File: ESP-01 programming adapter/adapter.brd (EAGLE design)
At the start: 27 x 27.3 mm, 7 parts

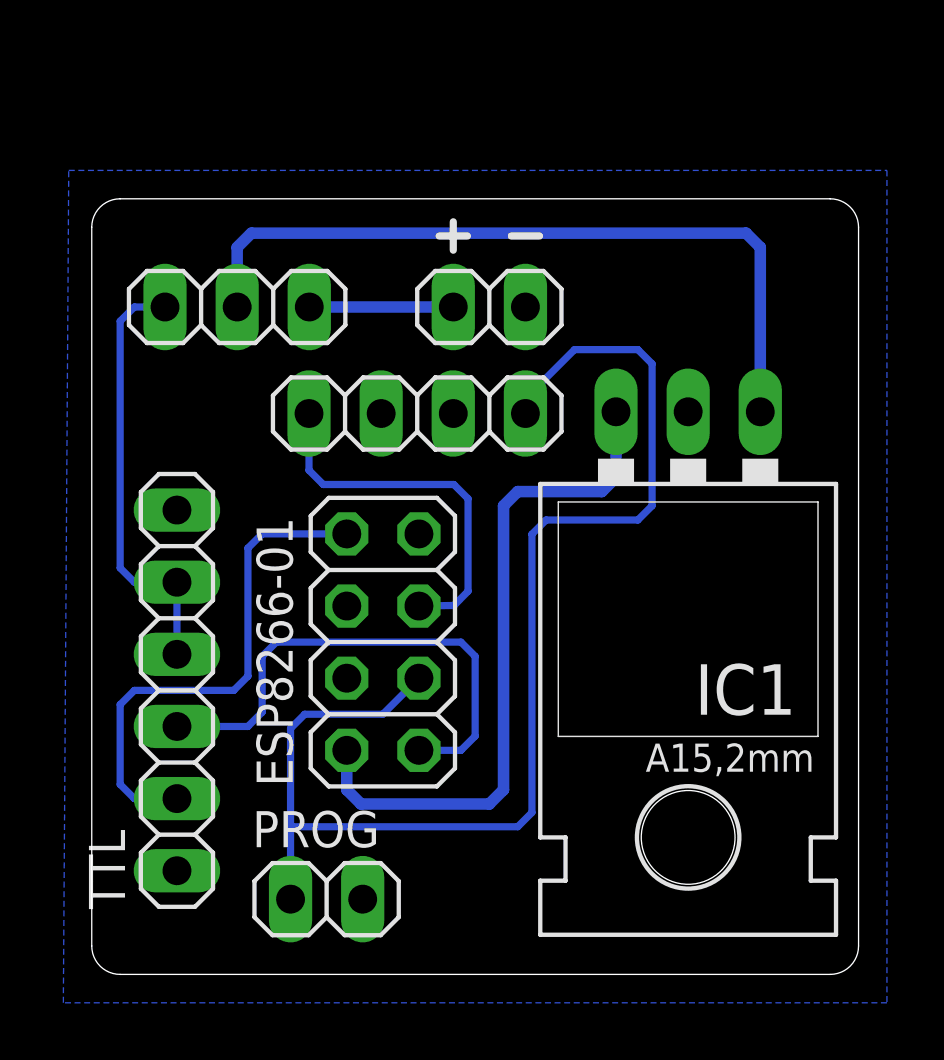
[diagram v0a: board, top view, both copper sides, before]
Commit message: CH_PD
Added resistor and jumper to the CH_PD pin, allowing for either
connecting it to VCC for constant on, or to connect it to GPIO00 for
controlling it by code.
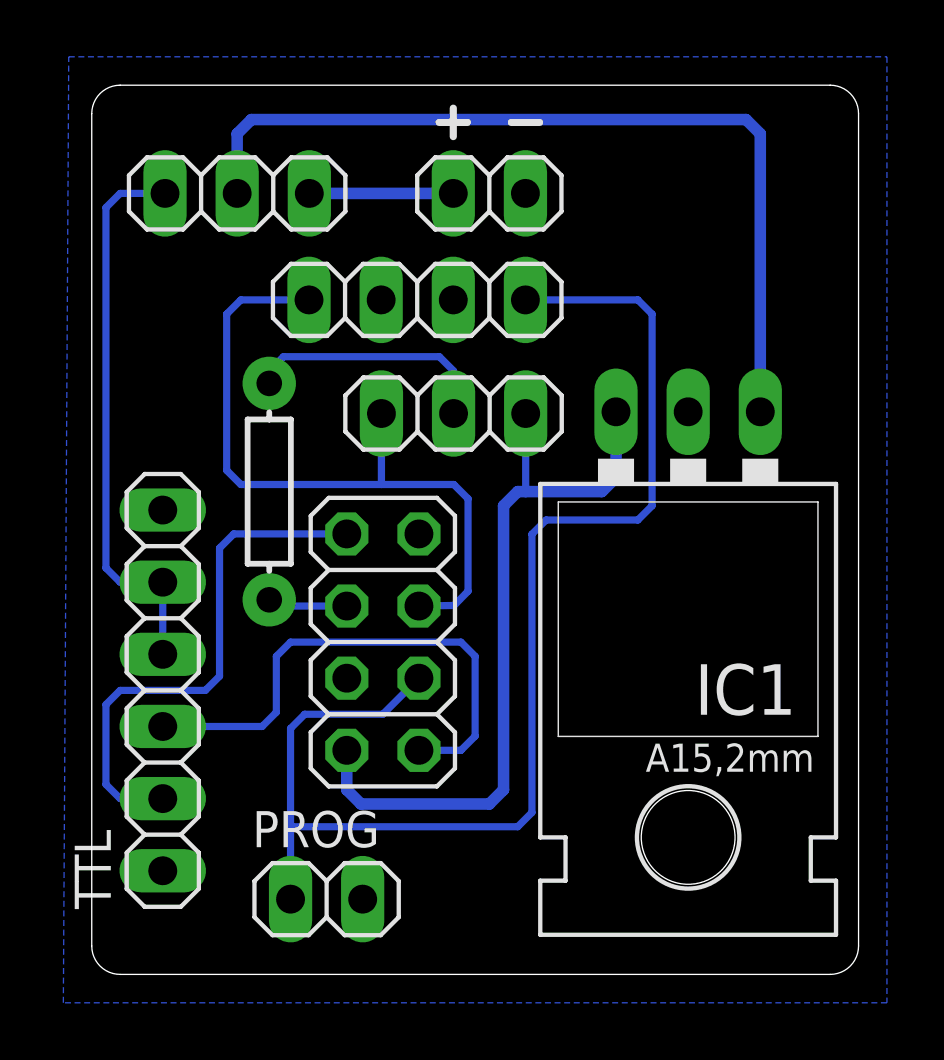
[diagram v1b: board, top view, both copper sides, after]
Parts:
- added R1: (no value), SparkFun-Resistors:AXIAL-0.3
- added V-SEL1: (no value), pinhead:1X03
- moved JP2 4.00 mm to (11.5, 23.8)
- moved V-SEL 4.00 mm to (5.12, 27.5)
- moved VIN 4.00 mm to (14.0, 27.5)
- moved TTL 0.50 mm to (2.50, 10.0)
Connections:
- new net N$10: R1.P$2, V-SEL1.2
- new net N$8: ESP8266-01.6, R1.P$1
- net N$1: now also V-SEL1.1
- net N$9: now also V-SEL1.3
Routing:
- net N$9: track 13.2 -> 25.2 mm
- net N$10: track 0.00 -> 8.84 mm
- net N$5: track 15.2 -> 19.7 mm
- net N$6: track 26.7 -> 30.7 mm
- net N$8: track 0.00 -> 2.95 mm
- net N$1: track 24.0 -> 26.8 mm
- net N$2: track 18.1 -> 18.6 mm
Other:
- board size 27 x 27.3 mm -> 27 x 31.3 mm

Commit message: Voltage regulator pin out
Changed pin out on the voltage regulator to fit TI LM1117 TO-220 package

http://www.ti.com/lit/ds/symlink/lm1117-n.pdf
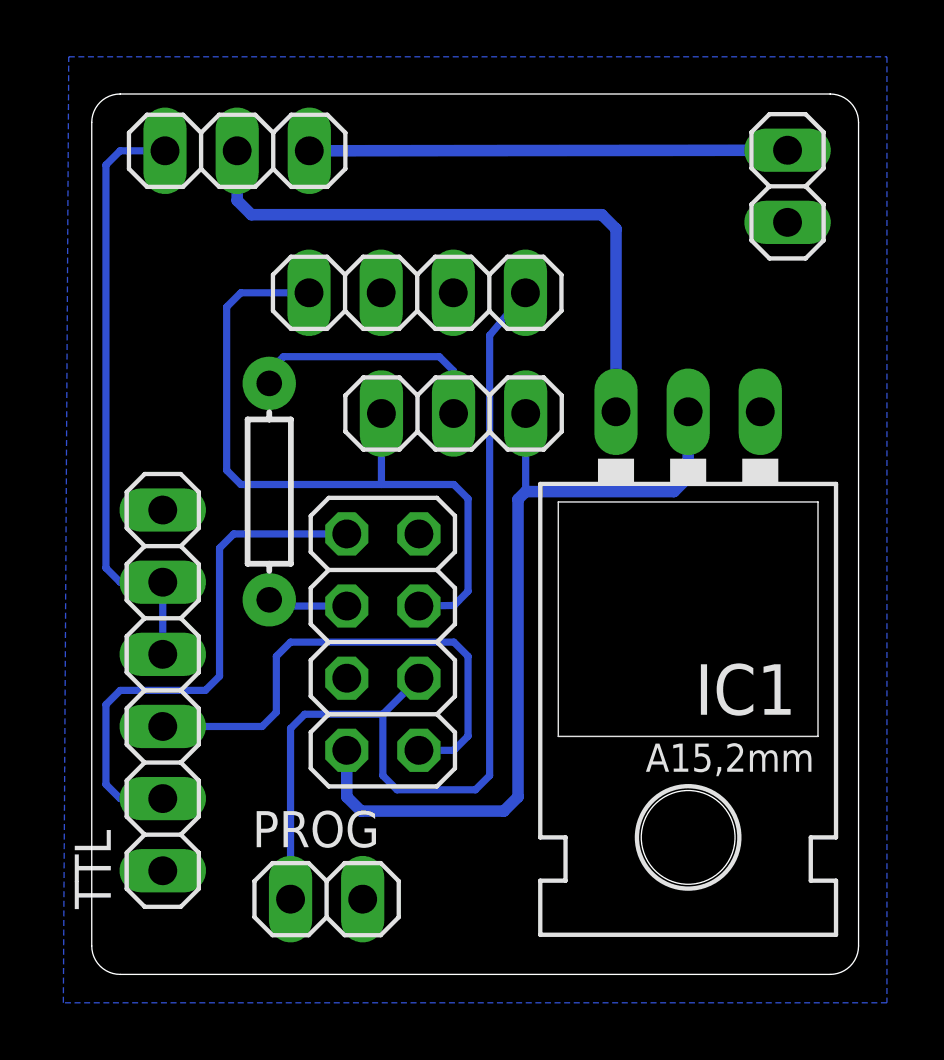
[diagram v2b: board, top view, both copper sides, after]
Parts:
- moved VIN 10.5 mm to (24.5, 27.8), turned to 270 degrees
- moved V-SEL 1.50 mm to (5.12, 29.0)
- moved JP2 0.25 mm to (11.5, 24.0)
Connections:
- removed net N$6: IC1.IN, V-SEL.2
- new net N$11: IC1.OUT, V-SEL.2
- net GND: now also IC1.IN; no longer IC1.GND
- net N$1: now also IC1.GND; no longer IC1.OUT
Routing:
- net N$6: track 30.7 -> 0.00 mm
- net N$11: track 0.00 -> 21.9 mm
- net N$7: track 5.07 -> 16.8 mm
- net N$4: track 45.8 -> 35.1 mm
- net N$1: track 26.8 -> 29.9 mm
- net N$5: track 19.7 -> 21.2 mm
- net N$3: track 18.6 -> 18.1 mm
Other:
- board size 27 x 31.3 mm -> 27 x 31 mm
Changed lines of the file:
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@@
 <board>
 <plain>
-<wire x1="0" y1="30.31" x2="0" y2="1" width="0" layer="20"/>
+<wire x1="0" y1="30" x2="0" y2="1" width="0" layer="20"/>
 <wire x1="0" y1="1" x2="1" y2="0" width="0" layer="20" curve="90"/>
 <wire x1="1" y1="0" x2="26" y2="0" width="0" layer="20"/>
 <wire x1="26" y1="0" x2="27" y2="1" width="0" layer="20" curve="90"/>
-<wire x1="27" y1="1" x2="27" y2="30.31" width="0" layer="20"/>
-<wire x1="27" y1="30.31" x2="26" y2="31.31" width="0" layer="20" curve="90"/>
-<wire x1="26" y1="31.31" x2="1" y2="31.31" width="0" layer="20"/>
-<wire x1="1" y1="31.31" x2="0" y2="30.31" width="0" layer="20" curve="90"/>
-<wire x1="14.77" y1="30" x2="15.77" y2="30" width="0.254" layer="25"/>
-<wire x1="12.23" y1="30" x2="13.23" y2="30" width="0.254" layer="25"/>
-<wire x1="12.73" y1="29.5" x2="12.73" y2="30.5" width="0.254" layer="25"/>
+<wire x1="27" y1="1" x2="27" y2="30" width="0" layer="20"/>
+<wire x1="27" y1="30" x2="26" y2="31" width="0" layer="20" curve="90"/>
+<wire x1="26" y1="31" x2="1" y2="31" width="0" layer="20"/>
+<wire x1="1" y1="31" x2="0" y2="30" width="0" layer="20" curve="90"/>
 </plain>
 <attributes>
@@
 </element>
 <element name="IC1" library="SparkFun-PowerIC" package="78XXL" value="" x="21" y="16" rot="R180"/>
-<element name="V-SEL" library="pinhead" package="1X03" value="" x="5.12" y="27.5" smashed="yes">
-<attribute name="VALUE" x="1.31" y="24.325" size="1.27" layer="27"/>
-</element>
-<element name="VIN" library="pinhead" package="1X02" value="" x="14" y="27.5" smashed="yes">
-<attribute name="VALUE" x="11.46" y="24.325" size="1.27" layer="27"/>
-</element>
-<element name="JP2" library="pinhead" package="1X04" value="" x="11.46" y="23.75" smashed="yes">
-<attribute name="VALUE" x="6.38" y="20.575" size="1.27" layer="27"/>
+<element name="V-SEL" library="pinhead" package="1X03" value="" x="5.12" y="29" smashed="yes">
+<attribute name="VALUE" x="1.31" y="25.825" size="1.27" layer="27"/>
+</element>
+<element name="VIN" library="pinhead" package="1X02" value="" x="24.5" y="27.75" smashed="yes" rot="R270">
+<attribute name="VALUE" x="21.325" y="30.29" size="1.27" layer="27" rot="R270"/>
+</element>
+<element name="JP2" library="pinhead" package="1X04" value="" x="11.46" y="24" smashed="yes">
+<attribute name="VALUE" x="6.38" y="20.825" size="1.27" layer="27"/>
 </element>
 <element name="R1" library="SparkFun-Resistors" package="AXIAL-0.3" value="" x="6.25" y="17" smashed="yes" rot="R90">
@@
 <vertex x="28" y="-1"/>
 </polygon>
-<contactref element="IC1" pad="GND"/>
 <contactref element="TTL" pad="1"/>
 <contactref element="ESP8266-01" pad="7"/>
@@
 <contactref element="JP2" pad="2"/>
 <contactref element="JP2" pad="3"/>
+<contactref element="IC1" pad="IN"/>
 </signal>
 <signal name="N$2">
@@
 <contactref element="TTL" pad="3"/>
 <contactref element="ESP8266-01" pad="1"/>
-<wire x1="13.5" y1="8.39" x2="13.5" y2="11.2" width="0.254" layer="16"/>
-<wire x1="13.5" y1="11.2" x2="13" y2="11.7" width="0.254" layer="16"/>
-<wire x1="13" y1="11.7" x2="7" y2="11.7" width="0.254" layer="16"/>
+<wire x1="13.25" y1="8.39" x2="13.25" y2="11.2" width="0.254" layer="16"/>
+<wire x1="13.25" y1="11.2" x2="12.75" y2="11.7" width="0.254" layer="16"/>
+<wire x1="12.75" y1="11.7" x2="7" y2="11.7" width="0.254" layer="16"/>
 <wire x1="7" y1="11.7" x2="6.5" y2="11.2" width="0.254" layer="16"/>
 <wire x1="2.5" y1="8.73" x2="6" y2="8.73" width="0.254" layer="16"/>
 <wire x1="6" y1="8.73" x2="6.5" y2="9.23" width="0.254" layer="16"/>
 <wire x1="6.5" y1="9.23" x2="6.5" y2="11.2" width="0.254" layer="16"/>
-<wire x1="11.52" y1="7.89" x2="13" y2="7.89" width="0.254" layer="16"/>
-<wire x1="13" y1="7.89" x2="13.5" y2="8.39" width="0.254" layer="16"/>
+<wire x1="11.52" y1="7.89" x2="12.75" y2="7.89" width="0.254" layer="16"/>
+<wire x1="12.75" y1="7.89" x2="13.25" y2="8.39" width="0.254" layer="16"/>
 </signal>
 <signal name="N$4">
@@
 <wire x1="10.25" y1="9.16" x2="7.5" y2="9.16" width="0.254" layer="16"/>
 <wire x1="7.5" y1="9.16" x2="7" y2="8.66" width="0.254" layer="16"/>
-<wire x1="7" y1="8.66" x2="7" y2="5.2" width="0.254" layer="16"/>
+<wire x1="7" y1="8.66" x2="7" y2="2.65" width="0.254" layer="16"/>
 <contactref element="JP2" pad="4"/>
-<wire x1="7" y1="5.2" x2="7" y2="2.65" width="0.254" layer="16"/>
-<wire x1="15.27" y1="23.75" x2="19.23" y2="23.75" width="0.254" layer="16"/>
-<wire x1="19.23" y1="23.75" x2="19.73" y2="23.25" width="0.254" layer="16"/>
-<wire x1="19.73" y1="23.25" x2="19.73" y2="16.5" width="0.254" layer="16"/>
-<wire x1="19.73" y1="16.5" x2="19.23" y2="16" width="0.254" layer="16"/>
-<wire x1="19.23" y1="16" x2="16" y2="16" width="0.254" layer="16"/>
-<wire x1="16" y1="16" x2="15.5" y2="15.5" width="0.254" layer="16"/>
-<wire x1="15.5" y1="15.5" x2="15.5" y2="5.7" width="0.254" layer="16"/>
-<wire x1="15.5" y1="5.7" x2="15" y2="5.2" width="0.254" layer="16"/>
-<wire x1="15" y1="5.2" x2="7" y2="5.2" width="0.254" layer="16"/>
+<wire x1="15.27" y1="24" x2="14.01" y2="22.5" width="0.254" layer="16"/>
+<wire x1="14.01" y1="22.5" x2="14.01" y2="7" width="0.254" layer="16"/>
+<wire x1="14.01" y1="7" x2="13.51" y2="6.5" width="0.254" layer="16"/>
+<wire x1="13.51" y1="6.5" x2="10.75" y2="6.5" width="0.254" layer="16"/>
+<wire x1="10.75" y1="6.5" x2="10.25" y2="7" width="0.254" layer="16"/>
+<wire x1="10.25" y1="7" x2="10.25" y2="9.16" width="0.254" layer="16"/>
 </signal>
 <signal name="N$1">
 <contactref element="ESP8266-01" pad="2"/>
-<contactref element="IC1" pad="OUT"/>
-<wire x1="14" y1="6" x2="9.48" y2="6" width="0.4064" layer="16"/>
-<wire x1="9.48" y1="6" x2="8.98" y2="6.5" width="0.4064" layer="16"/>
-<wire x1="8.98" y1="6.5" x2="8.98" y2="7.89" width="0.4064" layer="16"/>
-<wire x1="14" y1="6" x2="14.5" y2="6.5" width="0.4064" layer="16"/>
-<wire x1="14.5" y1="6.5" x2="14.5" y2="16.5" width="0.4064" layer="16"/>
-<wire x1="14.5" y1="16.5" x2="15" y2="17" width="0.4064" layer="16"/>
-<wire x1="15" y1="17" x2="15.28" y2="17" width="0.4064" layer="16"/>
-<wire x1="15.28" y1="17" x2="17.96" y2="17" width="0.4064" layer="16"/>
-<wire x1="17.96" y1="17" x2="18.46" y2="17.5" width="0.4064" layer="16"/>
-<wire x1="18.46" y1="17.5" x2="18.46" y2="19.81" width="0.4064" layer="16"/>
+<wire x1="9.48" y1="5.75" x2="14.51" y2="5.75" width="0.4064" layer="16"/>
+<wire x1="14.51" y1="5.75" x2="15.01" y2="6.25" width="0.4064" layer="16"/>
+<wire x1="15.01" y1="6.25" x2="15.01" y2="16.73" width="0.4064" layer="16"/>
+<wire x1="9.48" y1="5.75" x2="8.98" y2="6.25" width="0.4064" layer="16"/>
+<wire x1="8.98" y1="6.25" x2="8.98" y2="7.89" width="0.4064" layer="16"/>
+<wire x1="15.01" y1="16.73" x2="15.28" y2="17" width="0.4064" layer="16"/>
 <contactref element="V-SEL1" pad="1"/>
 <wire x1="15.28" y1="19.75" x2="15.28" y2="17" width="0.254" layer="16"/>
+<contactref element="IC1" pad="GND"/>
+<wire x1="15.28" y1="17" x2="20.5" y2="17" width="0.4064" layer="16"/>
+<wire x1="20.5" y1="17" x2="21" y2="17.5" width="0.4064" layer="16"/>
+<wire x1="21" y1="17.5" x2="21" y2="19.81" width="0.4064" layer="16"/>
 </signal>
 <signal name="N$5">
 <contactref element="TTL" pad="5"/>
 <contactref element="V-SEL" pad="1"/>
-<wire x1="2.58" y1="27.5" x2="1" y2="27.5" width="0.254" layer="16"/>
-<wire x1="1" y1="27.5" x2="0.5" y2="27" width="0.254" layer="16"/>
-<wire x1="0.5" y1="27" x2="0.5" y2="14.31" width="0.254" layer="16"/>
+<wire x1="2.58" y1="29" x2="1" y2="29" width="0.254" layer="16"/>
+<wire x1="1" y1="29" x2="0.5" y2="28.5" width="0.254" layer="16"/>
+<wire x1="0.5" y1="28.5" x2="0.5" y2="14.31" width="0.254" layer="16"/>
 <wire x1="0.5" y1="14.31" x2="1" y2="13.81" width="0.254" layer="16"/>
 <wire x1="1" y1="13.81" x2="2.5" y2="13.81" width="0.254" layer="16"/>
@@
 <wire x1="2.5" y1="13.81" x2="2.5" y2="11.27" width="0.254" layer="16"/>
 </signal>
-<signal name="N$6">
-<contactref element="V-SEL" pad="2"/>
-<contactref element="IC1" pad="IN"/>
-<wire x1="5.12" y1="27.5" x2="5.12" y2="29.6" width="0.4064" layer="16"/>
-<wire x1="5.12" y1="29.6" x2="5.62" y2="30.1" width="0.4064" layer="16"/>
-<wire x1="5.62" y1="30.1" x2="23.04" y2="30.1" width="0.4064" layer="16"/>
-<wire x1="23.54" y1="19.81" x2="23.54" y2="29.6" width="0.4064" layer="16"/>
-<wire x1="23.54" y1="29.6" x2="23.04" y2="30.1" width="0.4064" layer="16"/>
-</signal>
 <signal name="N$7">
 <contactref element="V-SEL" pad="3"/>
 <contactref element="VIN" pad="1"/>
-<wire x1="7.66" y1="27.5" x2="12.73" y2="27.5" width="0.4064" layer="16"/>
+<wire x1="7.66" y1="29" x2="24.5" y2="29.02" width="0.4064" layer="16"/>
 </signal>
 <signal name="N$9">
@@
 <wire x1="10.2" y1="17.25" x2="5.25" y2="17.25" width="0.254" layer="16"/>
 <wire x1="5.25" y1="17.25" x2="4.75" y2="17.75" width="0.254" layer="16"/>
-<wire x1="4.75" y1="17.75" x2="4.75" y2="23.25" width="0.254" layer="16"/>
-<wire x1="4.75" y1="23.25" x2="5.25" y2="23.75" width="0.254" layer="16"/>
-<wire x1="5.25" y1="23.75" x2="7.65" y2="23.75" width="0.254" layer="16"/>
+<wire x1="4.75" y1="17.75" x2="4.75" y2="23.5" width="0.254" layer="16"/>
+<wire x1="4.75" y1="23.5" x2="5.25" y2="24" width="0.254" layer="16"/>
+<wire x1="5.25" y1="24" x2="7.65" y2="24" width="0.254" layer="16"/>
 </signal>
 <signal name="N$8">
@@
 <wire x1="12.74" y1="21.25" x2="12.74" y2="19.75" width="0.254" layer="16"/>
 </signal>
+<signal name="N$11">
+<contactref element="V-SEL" pad="2"/>
+<contactref element="IC1" pad="OUT"/>
+<wire x1="18.46" y1="19.81" x2="18.46" y2="26.25" width="0.4064" layer="16"/>
+<wire x1="18.46" y1="26.25" x2="17.96" y2="26.75" width="0.4064" layer="16"/>
+<wire x1="17.96" y1="26.75" x2="5.62" y2="26.75" width="0.4064" layer="16"/>
+<wire x1="5.62" y1="26.75" x2="5.12" y2="27.25" width="0.4064" layer="16"/>
+<wire x1="5.12" y1="27.25" x2="5.12" y2="29" width="0.4064" layer="16"/>
+</signal>
 </signals>
